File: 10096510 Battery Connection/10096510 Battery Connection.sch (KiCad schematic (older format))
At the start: 27 parts, among them J1 09185107323, J3 811-S1-002-30-014101, J4 811-S1-002-30-014101, J5 811-S1-002-30-014101, J6 GKS-913-0024

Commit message: Libraries nicknames update in Kicad projects
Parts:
- C1, C2: symbol Capacitor:0603_10nF_CC0603KRX7R9BB103 -> V_Capacitor:0603_10nF_CC0603KRX7R9BB103
- C3, C4: symbol Capacitor:0402_47pF_C0402C470J5GAC -> V_Capacitor:0402_47pF_C0402C470J5GAC
- FI1: symbol Inductor:BNX002-11 -> V_Inductor:BNX002-11
- FI2, FI3: symbol Inductor:74279266 -> V_Inductor:74279266
- J1: symbol Connector:09185107323 -> V_Connector:09185107323
- J3, J4, J5: symbol Connector:811-S1-002-30-014101 -> V_Connector:811-S1-002-30-014101
- J6: symbol Connector:GKS-913-0024 -> V_Connector:GKS-913-0024
- PT1, PT2: symbol Connector:TestPoint -> V_Connector:TestPoint
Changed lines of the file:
@@
 	2250 4500 2250 4400
 $Comp
-L Capacitor:0402_47pF_C0402C470J5GAC C3
+L V_Capacitor:0402_47pF_C0402C470J5GAC C3
 U 1 1 5E91F4F8
 P 6600 3950
@@
 $EndComp
 $Comp
-L Capacitor:0402_47pF_C0402C470J5GAC C4
+L V_Capacitor:0402_47pF_C0402C470J5GAC C4
 U 1 1 5E9213A5
 P 6600 4800
@@
 ADVANCED CONTACT\nTO ENSURE GROUND CONTACT FIRST
 $Comp
-L Power:GND #PWR0101
+L V_Power:GND #PWR0101
 U 1 1 5E92D67C
 P 7200 5650
@@
 	7200 5500 7450 5500
 $Comp
-L Power:GND #PWR0102
+L V_Power:GND #PWR0102
 U 1 1 5E92FBCB
 P 6600 5000
@@
 	6600 5000 6600 4950
 $Comp
-L Power:GND #PWR0103
+L V_Power:GND #PWR0103
 U 1 1 5E930F1A
 P 6600 4150
@@
 	1150 3750 1150 4600
 $Comp
-L Connector:09185107323 J1
+L V_Connector:09185107323 J1
 U 1 1 5E95772A
 P 2700 4600
@@
 $EndComp
 $Comp
-L Power:Earth #PWR0104
+L V_Power:Earth #PWR0104
 U 1 1 5E96166B
 P 2650 5000
@@
 	2900 4800 3000 4800
 $Comp
-L Power:VDD #PWR0105
+L V_Power:VDD #PWR0105
 U 1 1 5E977E9C
 P 2650 4000
@@
 	4850 2050 4850 2250
 $Comp
-L Power:VDD #PWR0106
+L V_Power:VDD #PWR0106
 U 1 1 5E981F53
 P 4850 2050
@@
 	4850 3050 4850 2650
 $Comp
-L Power:Earth #PWR0107
+L V_Power:Earth #PWR0107
 U 1 1 5E95EC8B
 P 4850 3050
@@
 	6550 3050 6550 2950
 $Comp
-L Power:GND #PWR0108
+L V_Power:GND #PWR0108
 U 1 1 5E959A23
 P 6550 3050
@@
 	5050 2250 4850 2250
 $Comp
-L Capacitor:0603_10nF_CC0603KRX7R9BB103 C1
+L V_Capacitor:0603_10nF_CC0603KRX7R9BB103 C1
 U 1 1 5E8FB3FB
 P 4850 2450
@@
 $EndComp
 $Comp
-L Inductor:BNX002-11 FI1
+L V_Inductor:BNX002-11 FI1
 U 1 1 5E8EDF96
 P 5600 2350
@@
 	7450 2250 7300 2250
 $Comp
-L Connector:811-S1-002-30-014101 J4
+L V_Connector:811-S1-002-30-014101 J4
 U 1 1 5E99CA09
 P 7450 3750
@@
 $EndComp
 $Comp
-L Connector:811-S1-002-30-014101 J5
+L V_Connector:811-S1-002-30-014101 J5
 U 1 1 5E99E657
 P 7450 4600
@@
 GND
 $Comp
-L Connector:GKS-913-0024 J6
+L V_Connector:GKS-913-0024 J6
 U 1 1 5E9A6A5B
 P 7450 5500
@@
 	2250 4800 2400 4800
 $Comp
-L Inductor:74279266 FI3
+L V_Inductor:74279266 FI3
 U 1 1 5E9C95BC
 P 3350 4600
@@
 	1950 4600 2400 4600
 $Comp
-L Capacitor:0603_10nF_CC0603KRX7R9BB103 C2
+L V_Capacitor:0603_10nF_CC0603KRX7R9BB103 C2
 U 1 1 5E90C557
 P 6550 2450
@@
 $EndComp
 $Comp
-L Inductor:74279266 FI2
+L V_Inductor:74279266 FI2
 U 1 1 5E9D0294
 P 1800 4600
@@
 $EndComp
 $Comp
-L Connector:811-S1-002-30-014101 J3
+L V_Connector:811-S1-002-30-014101 J3
 U 1 1 5E99A69C
 P 7450 2250
@@
 $EndComp
 $Comp
-L Connector:TestPoint PT1
+L V_Connector:TestPoint PT1
 U 1 1 5E9E685B
 P 1650 6550
@@
 $EndComp
 $Comp
-L Connector:TestPoint PT2
+L V_Connector:TestPoint PT2
 U 1 1 5E9E73E6
 P 1650 7000
@@
 $EndComp
 $Comp
-L Power:GND #PWR0109
+L V_Power:GND #PWR0109
 U 1 1 5EA02F7C
 P 1650 6550
@@
 $EndComp
 $Comp
-L Power:GND #PWR0110
+L V_Power:GND #PWR0110
 U 1 1 5EA04F8B
 P 1650 7000
@@
 $EndComp
 $Comp
-L Power:PWR_FLAG #FLG0103
+L V_Power:PWR_FLAG #FLG0103
 U 1 1 5EA3D24A
 P 6550 3050

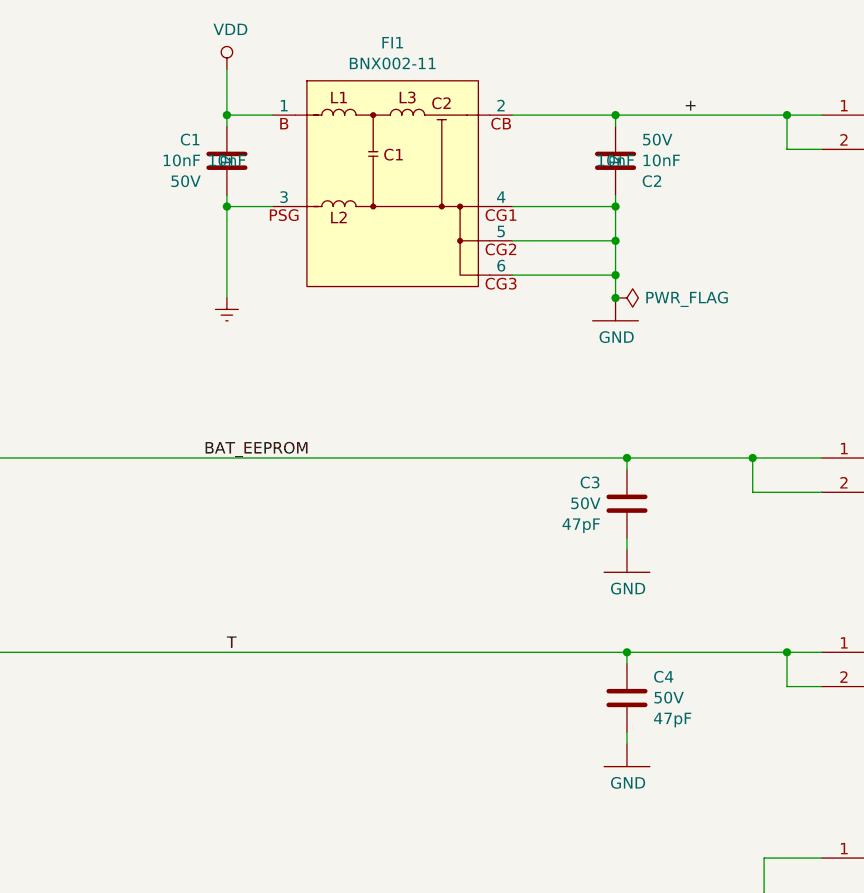
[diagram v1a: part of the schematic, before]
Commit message: Battery Conn: fields updated from library, non-library fields removed
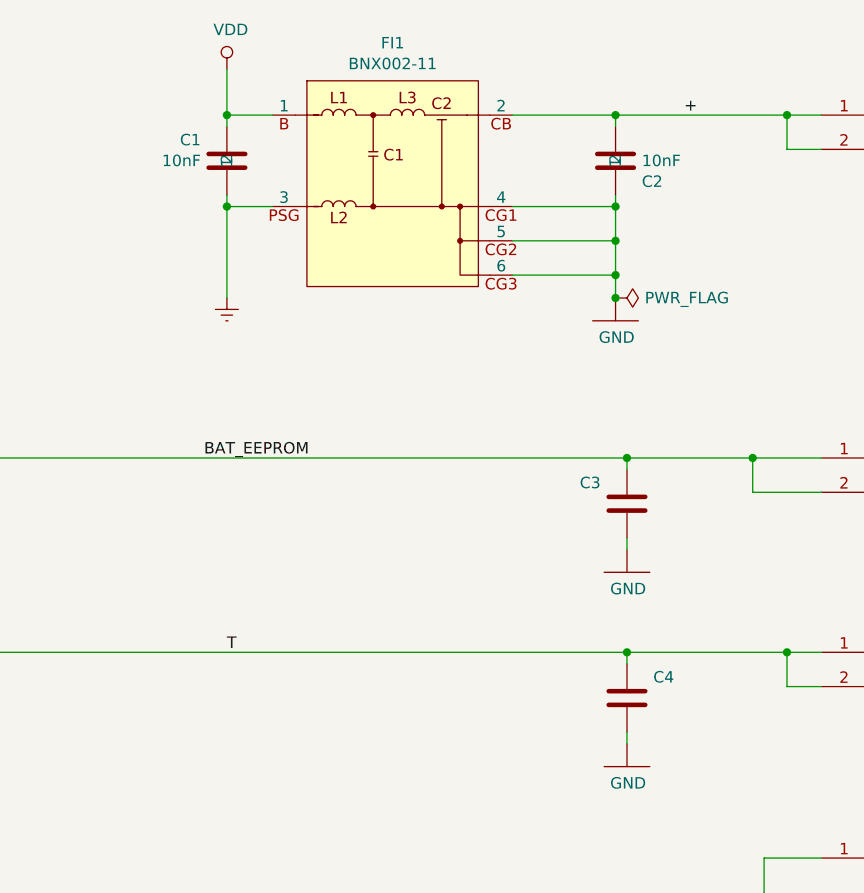
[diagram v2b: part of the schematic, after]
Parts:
- C1, C2: CAP_VAL 10nF -> (none); Description (none) -> CAPACITOR CERAMIC,10NF,+/-10%,50V,0603; Documentation ${KIPRJMOD}/Datasheets/YAGEO_CC0603KRX7R9BB103.pdf -> (none); Manufacturer Yageo -> YAGEO_RMS1; Manufacturer2 (none) -> YAGEO_RMS1; Manufacturer3 (none) -> KEMET_RMS1; Manufacturer_No2 (none) -> CC0603JRX7R9BB103; Manufacturer_No3 (none) -> C0603C103K5RACTU; Size 0603 -> (none); Voltage 50V -> (none)
- C3, C4: CAP_VAL 47pF -> (none); Description (none) -> CAPACITOR,47 PF,+/-5%,50V,0402; Documentation ${KIPRJMOD}/Datasheets/KEMET_C0402C470J5GAC.pdf -> (none); Manufacturer Kemet -> KEMET_RMS1; Manufacturer2 (none) -> SAMSUNG_RMS1; Manufacturer3 (none) -> MURATA MANUFACTURING CO., LTD.; Manufacturer_No2 (none) -> CL05C470JB5NNNC; Manufacturer_No3 (none) -> GRM1555C1H470JA01D; Size 0402 -> (none); Voltage 50V -> (none)
- FI1: Description (none) -> FILTER CC, 1MHZ-1GHZ, 10A, 50V; Documentation ${KIPRJMOD}/Datasheets/MURATA_BNX002-11.pdf -> (none); Manufacturer Murata -> MURATA MANUFACTURING CO., LTD.; Manufacturer2 (none) -> MURATA MANUFACTURING CO., LTD.; Manufacturer3 (none) -> MURATA MANUFACTURING CO., LTD.; Manufacturer_No BNX002-11 -> BNX002-01; Manufacturer_No2 (none) -> BNX00201; Manufacturer_No3 (none) -> BNX002-11
- FI2, FI3: Current Rating 200mA -> (none); Description (none) -> SMD FERRITE 200MA; Documentation ${KIPRJMOD}/Datasheets/WURTH_74279266.pdf -> (none); Height 1.00mm -> (none); Impedance 1kohm_at_100MHz -> (none); Manufacturer Wurth Elektronik -> WURTH ELEKTRONIK GMBH; Package 0603 -> (none)
- J1: Description (none) -> CONNECTOR, 10 CONTACTS, HE10; Documentation ${KIPRJMOD}/Datasheets/HARTING_09185107323.pdf -> (none); Manufacturer Harting -> HARTING
- J3, J4, J5: Description CONN SPRING PISTON 2POS SMD -> CONNECTOR, 2 CONTACTS, PIN SPACE 2.54, SM; Documentation ${KIPRJMOD}/Datasheets/PRECI-DIP_811-S1-002-30-014101.pdf -> (none); Height 6mm -> (none); Manufacturer Preci-Dip -> PRECI-DIP (015220)
- J6: Description Test probe -> CONNECTOR, 1 CONTACTS, TEST PROBE; Documentation ${KIPRJMOD}/Datasheets/INGUN_GKS-913 305 230 A 1502 S.pdf -> (none); Manufacturer Ingun -> INGUN; Manufacturer2 (none) -> INGUN; Manufacturer_No GKS-913 305 230 A 1502 S -> GKS-913 305 230 A 15 02 S; Manufacturer_No2 (none) -> GKS-913-0024
- PT1, PT2: Description (none) -> TEST POINT; Item Number (none) -> 10022924; Manufacturer (none) -> NICOMATIC_RMS1; Manufacturer2 (none) -> KEYSTONE ELECTRONICS CORP; Manufacturer_No (none) -> C12000B; Manufacturer_No2 (none) -> 5015

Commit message: Renamed FLTR.lib to Filter.lib, created V_Mechanical
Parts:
- CAM1, CAM10, CAM11, CAM12, CAM14, CAM16, CAM2, CAM3, CAM4, CAM6, CAM7, CAM8, CAM9: symbol Mechanical:Fiducial -> V_Mechanical:Fiducial
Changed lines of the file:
@@
 $EndComp
 $Comp
-L Mechanical:Fiducial CAM1
+L V_Mechanical:Fiducial CAM1
 U 1 1 5E9EFCDE
 P 2700 6400
@@
 $EndComp
 $Comp
-L Mechanical:Fiducial CAM2
+L V_Mechanical:Fiducial CAM2
 U 1 1 5E9F043D
 P 2700 6550
@@
 $EndComp
 $Comp
-L Mechanical:Fiducial CAM3
+L V_Mechanical:Fiducial CAM3
 U 1 1 5E9F1828
 P 2700 6700
@@
 $EndComp
 $Comp
-L Mechanical:Fiducial CAM4
+L V_Mechanical:Fiducial CAM4
 U 1 1 5E9F1832
 P 2700 6850
@@
 $EndComp
 $Comp
-L Mechanical:Fiducial CAM6
+L V_Mechanical:Fiducial CAM6
 U 1 1 5E9F54AD
 P 2700 7150
@@
 $EndComp
 $Comp
-L Mechanical:Fiducial CAM7
+L V_Mechanical:Fiducial CAM7
 U 1 1 5E9F54B7
 P 2700 7300
@@
 $EndComp
 $Comp
-L Mechanical:Fiducial CAM8
+L V_Mechanical:Fiducial CAM8
 U 1 1 5E9F54C1
 P 2700 7450
@@
 $EndComp
 $Comp
-L Mechanical:Fiducial CAM9
+L V_Mechanical:Fiducial CAM9
 U 1 1 5E9FC9D9
 P 3150 6400
@@
 $EndComp
 $Comp
-L Mechanical:Fiducial CAM10
+L V_Mechanical:Fiducial CAM10
 U 1 1 5E9FC9E3
 P 3150 6550
@@
 $EndComp
 $Comp
-L Mechanical:Fiducial CAM11
+L V_Mechanical:Fiducial CAM11
 U 1 1 5E9FC9ED
 P 3150 6700
@@
 $EndComp
 $Comp
-L Mechanical:Fiducial CAM12
+L V_Mechanical:Fiducial CAM12
 U 1 1 5E9FC9F7
 P 3150 6850
@@
 $EndComp
 $Comp
-L Mechanical:Fiducial CAM14
+L V_Mechanical:Fiducial CAM14
 U 1 1 5E9FCA0B
 P 3150 7150
@@
 $EndComp
 $Comp
-L Mechanical:Fiducial CAM16
+L V_Mechanical:Fiducial CAM16
 U 1 1 5E9FCA1F
 P 3150 7450

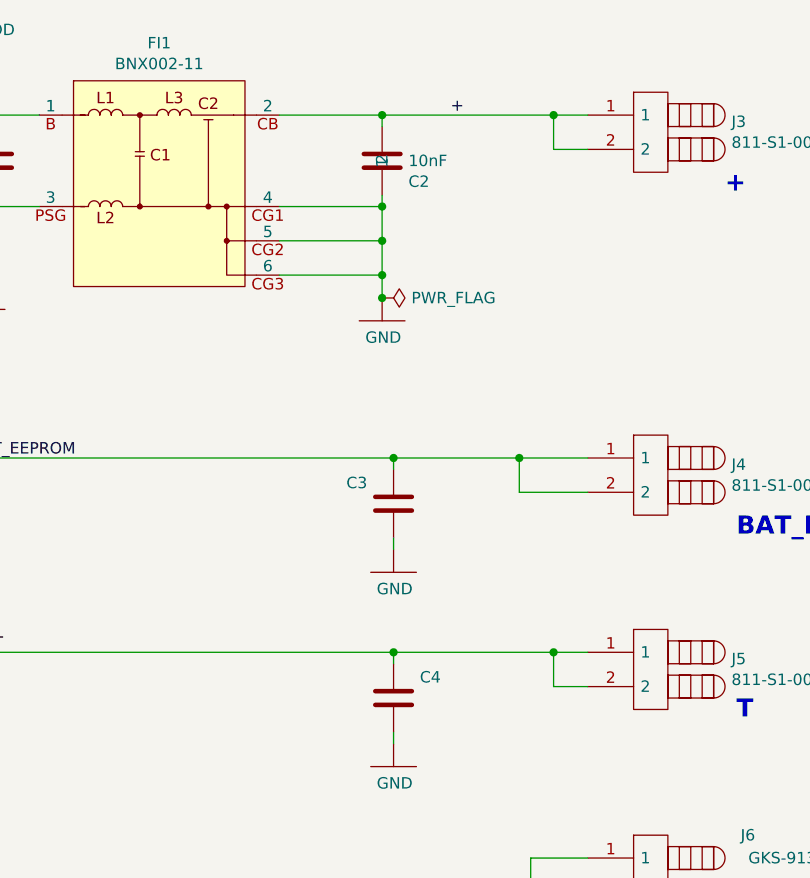
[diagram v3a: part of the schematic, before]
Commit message: Battery connection: fields corrections on schematics
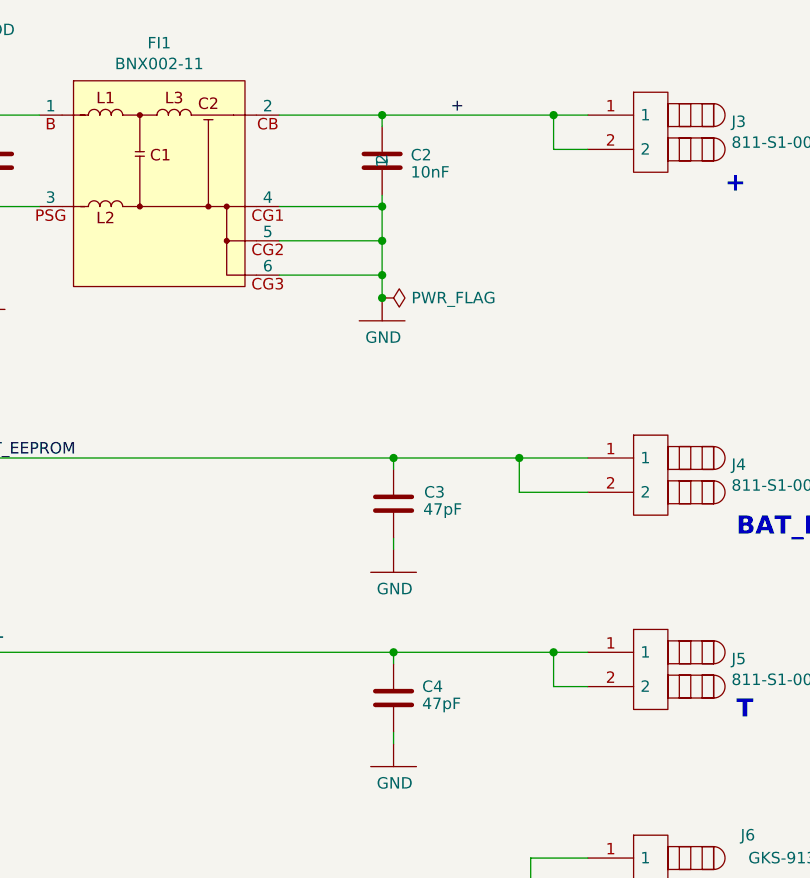
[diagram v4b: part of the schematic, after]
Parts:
- C3, C4: value 0402_47pF_C0402C470J5GAC -> 47pF
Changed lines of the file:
@@
 U 1 1 5E91F4F8
 P 6600 3950
-F 0 "C3" H 6715 4041 50  0000 L CNN
-F 1 "0402_47pF_C0402C470J5GAC" H 6950 3750 50  0001 L CNN
+F 0 "C3" H 6375 4000 50  0000 L CNN
+F 1 "47pF" H 6300 3925 50  0000 L CNN
 F 2 "AllModules:C0402_1b" H 7600 3850 50  0001 C CNN
 F 3 "" H 6600 3950 50  0001 C CNN
@@
 U 1 1 5E9213A5
 P 6600 4800
-F 0 "C4" H 6715 4891 50  0000 L CNN
-F 1 "0402_47pF_C0402C470J5GAC" H 6950 4600 50  0001 L CNN
+F 0 "C4" H 6725 4850 50  0000 L CNN
+F 1 "47pF" H 6725 4775 50  0000 L CNN
 F 2 "AllModules:C0402_1b" H 7600 4700 50  0001 C CNN
 F 3 "" H 6600 4800 50  0001 C CNN
@@
 F 7 "FILTER CC, 1MHZ-1GHZ, 10A, 50V" H 0   0   50  0001 C CNN "Description"
 F 8 "MURATA MANUFACTURING CO., LTD." H 0   0   50  0001 C CNN "Manufacturer2"
-F 9 "MURATA MANUFACTURING CO., LTD." H 0   0   50  0001 C CNN "Manufacturer3"
-F 10 "BNX00201" H 0   0   50  0001 C CNN "Manufacturer_No2"
+F 9 "BNX00201" H 0   0   50  0001 C CNN "Manufacturer_No2"
+F 10 "MURATA MANUFACTURING CO., LTD." H 0   0   50  0001 C CNN "Manufacturer3"
 F 11 "BNX002-11" H 0   0   50  0001 C CNN "Manufacturer_No3"
 	1    5600 2350
 	1    0    0    -1
 $EndComp
-Wire Wire Line
-	7450 2400 7300 2400
-Wire Wire Line
-	7450 2250 7300 2250
 $Comp
 L V_Connector:811-S1-002-30-014101 J4
@@
 	1950 4600 2400 4600
 $Comp
-L V_Capacitor:0603_10nF_CC0603KRX7R9BB103 C2
-U 1 1 5E90C557
-P 6550 2450
-F 0 "C2" H 6665 2541 50  0000 L CNN
-F 1 "10nF" H 6665 2450 50  0000 L CNN
-F 2 "AllModules:C0603_1b" H 7550 2250 50  0001 C CNN
-F 3 "" H 6550 2450 50  0001 C CNN
-F 4 "YAGEO_RMS1" H 7000 2550 50  0001 C CNN "Manufacturer"
-F 5 "10022508" H 0   0   50  0001 C CNN "Item Number"
-F 6 "CC0603KRX7R9BB103" H 0   0   50  0001 C CNN "Manufacturer_No"
-F 7 "CAPACITOR CERAMIC,10NF,+/-10%,50V,0603" H 0   0   50  0001 C CNN "Description"
-F 8 "YAGEO_RMS1" H 0   0   50  0001 C CNN "Manufacturer2"
-F 9 "KEMET_RMS1" H 0   0   50  0001 C CNN "Manufacturer3"
-F 10 "CC0603JRX7R9BB103" H 0   0   50  0001 C CNN "Manufacturer_No2"
-F 11 "C0603C103K5RACTU" H 0   0   50  0001 C CNN "Manufacturer_No3"
-	1    6550 2450
-	1    0    0    1
-$EndComp
-$Comp
 L V_Inductor:74279266 FI2
 U 1 1 5E9D0294
@@
 F 7 "SMD FERRITE 200MA" H 0   0   50  0001 C CNN "Description"
 	1    1800 4600
-	1    0    0    -1
-$EndComp
-$Comp
-L V_Connector:811-S1-002-30-014101 J3
-U 1 1 5E99A69C
-P 7450 2250
-F 0 "J3" H 8078 2221 50  0000 L CNN
-F 1 "811-S1-002-30-014101" H 8078 2130 50  0000 L CNN
-F 2 "AllModules:811S1-02_1" H 8100 2350 50  0001 L CNN
-F 3 "" H 8100 2250 50  0001 L CNN
-F 4 "CONNECTOR, 2 CONTACTS, PIN SPACE 2.54, SM" H 8100 2250 50  0001 L CNN "Description"
-F 5 "PRECI-DIP                       (015220)" H 8100 2050 50  0001 L CNN "Manufacturer"
-F 6 "10023420" H 0   0   50  0001 C CNN "Item Number"
-F 7 "811-S1-002-30-014101" H 0   0   50  0001 C CNN "Manufacturer_No"
-	1    7450 2250
 	1    0    0    -1
 $EndComp
@@
 $EndComp
 Connection ~ 6550 3050
+Wire Wire Line
+	7450 2400 7300 2400
+Wire Wire Line
+	7450 2250 7300 2250
+$Comp
+L V_Connector:811-S1-002-30-014101 J3
+U 1 1 5E99A69C
+P 7450 2250
+F 0 "J3" H 8078 2221 50  0000 L CNN
+F 1 "811-S1-002-30-014101" H 8078 2130 50  0000 L CNN
+F 2 "AllModules:811S1-02_1" H 8100 2350 50  0001 L CNN
+F 3 "" H 8100 2250 50  0001 L CNN
+F 4 "CONNECTOR, 2 CONTACTS, PIN SPACE 2.54, SM" H 8100 2250 50  0001 L CNN "Description"
+F 5 "PRECI-DIP                       (015220)" H 8100 2050 50  0001 L CNN "Manufacturer"
+F 6 "10023420" H 0   0   50  0001 C CNN "Item Number"
+F 7 "811-S1-002-30-014101" H 0   0   50  0001 C CNN "Manufacturer_No"
+	1    7450 2250
+	1    0    0    -1
+$EndComp
+$Comp
+L V_Capacitor:0603_10nF_CC0603KRX7R9BB103 C2
+U 1 1 5E90C557
+P 6550 2450
+F 0 "C2" H 6675 2425 50  0000 L CNN
+F 1 "10nF" H 6675 2500 50  0000 L CNN
+F 2 "AllModules:C0603_1b" H 7550 2250 50  0001 C CNN
+F 3 "" H 6550 2450 50  0001 C CNN
+F 4 "YAGEO_RMS1" H 7000 2550 50  0001 C CNN "Manufacturer"
+F 5 "10022508" H 0   0   50  0001 C CNN "Item Number"
+F 6 "CC0603KRX7R9BB103" H 0   0   50  0001 C CNN "Manufacturer_No"
+F 7 "CAPACITOR CERAMIC,10NF,+/-10%,50V,0603" H 0   0   50  0001 C CNN "Description"
+F 8 "YAGEO_RMS1" H 0   0   50  0001 C CNN "Manufacturer2"
+F 9 "KEMET_RMS1" H 0   0   50  0001 C CNN "Manufacturer3"
+F 10 "CC0603JRX7R9BB103" H 0   0   50  0001 C CNN "Manufacturer_No2"
+F 11 "C0603C103K5RACTU" H 0   0   50  0001 C CNN "Manufacturer_No3"
+	1    6550 2450
+	1    0    0    1
+$EndComp
 $EndSCHEMATC
